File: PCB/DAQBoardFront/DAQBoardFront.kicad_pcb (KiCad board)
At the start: 2 copper layers, 59.9 x 60.2 mm, 42 parts, among them IC2 LMR51430YDDCR, J2 53375-0410, U5 TCAN1051VDRQ1

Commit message: Updated A-A filters w/ final version, updated BOM
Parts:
- C8: value C3216X5R1E476M160AC -> C3216X5R1E476MTJ00E
- L1, L2: value 10u -> 22u
- L3: value L -> 22u
- R1, R2: value 1.69k -> 6.57k
- R3: value R -> 26.4k
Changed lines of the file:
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@@
 			(layer "F.SilkS")
 		)
+		(fp_rect
+			(start -3 -2.5)
+			(end 18 51)
+			(stroke
+				(width 0.1)
+				(type solid)
+			)
+			(fill no)
+			(layer "F.CrtYd")
+		)
 		(fp_text user "${REFERENCE}"
 			(at 7.64 6.7 0)
@@
 			)
 		)
-		(property "Description" "Resistor, 60Ohm, 1%, 1/4W"
+		(property "Description" "RCS060359R0FKEA"
 			(at 0 0 90)
 			(layer "B.Fab")
@@
 			)
 		)
-		(attr smd)
+		(attr smd dnp)
 		(duplicate_pad_numbers_are_jumpers no)
 		(fp_line
@@
 			)
 		)
-		(property "Value" "C3216X5R1E476M160AC"
+		(property "Value" "C3216X5R1E476MTJ00E"
 			(at 0 -1.85 90)
 			(layer "B.Fab")
@@
 			)
 		)
-		(property "Value" "10u"
+		(property "Value" "22u"
 			(at 0 -1.55 90)
 			(layer "B.Fab")
@@
 			)
 		)
-		(property "Value" "1.69k"
+		(property "Value" "6.57k"
 			(at 0 -1.43 90)
 			(layer "B.Fab")
@@
 			)
 		)
-		(property "Description" "Resistor, 60Ohm, 1%, 1/4W"
+		(property "Description" "RCS060359R0FKEA"
 			(at 0 0 90)
 			(layer "B.Fab")
@@
 			)
 		)
-		(attr smd)
+		(attr smd dnp)
 		(duplicate_pad_numbers_are_jumpers no)
 		(fp_line
@@
 			)
 		)
-		(property "Value" "R"
+		(property "Value" "26.4k"
 			(at 0 -1.43 90)
 			(layer "B.Fab")
@@
 		)
 		(pad "2" smd rect
-			(at 1.15 0 180)
+			(at 1.15 0)
 			(size 0.42 0.82)
 			(layers "B.Cu" "B.Mask" "B.Paste")
@@
 			)
 		)
-		(property "Value" "10u"
+		(property "Value" "22u"
 			(at 0 -1.5 90)
 			(layer "B.Fab")
@@
 			)
 		)
-		(property "Value" "1.69k"
+		(property "Value" "6.57k"
 			(at 0 -1.43 90)
 			(layer "B.Fab")
@@
 			)
 		)
-		(property "Value" "L"
+		(property "Value" "22u"
 			(at 0 -1.55 90)
 			(layer "B.Fab")

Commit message: Finalized A-A filters, finishing touches on DAQ and Dash boards
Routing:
- net /GND: vias 18 -> 26
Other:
- board text added: "A-A Filters"
- board text added: "CAN Transceiver"
- board text added: "Current Sense"
- board text added: "Volt Step-Dn"
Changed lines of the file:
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@@
 		(tags "capacitor")
 		(property "Reference" "C1"
-			(at -0.05 -1.5 0)
+			(at -2.3 0.6 0)
 			(layer "B.SilkS")
 			(effects
@@
 	)
 	(gr_rect
+		(start 99.45 69.1)
+		(end 119.9 81.3)
+		(stroke
+			(width 0.1)
+			(type default)
+		)
+		(fill no)
+		(layer "B.SilkS")
+	)
+	(gr_rect
+		(start 105.45 81.4)
+		(end 125.9 101.9)
+		(stroke
+			(width 0.1)
+			(type default)
+		)
+		(fill no)
+		(layer "B.SilkS")
+	)
+	(gr_rect
+		(start 135.65 100.8)
+		(end 157.2 124.3)
+		(stroke
+			(width 0.1)
+			(type default)
+		)
+		(fill no)
+		(layer "B.SilkS")
+	)
+	(gr_rect
+		(start 136.35 75.35)
+		(end 157.5 97.8)
+		(stroke
+			(width 0.1)
+			(type default)
+		)
+		(fill no)
+		(layer "B.SilkS")
+	)
+	(gr_rect
 		(start 98.5 67.9)
 		(end 158.45 128.05)
@@
 		(layer "F.CrtYd")
 	)
+	(gr_text "CAN Transceiver"
+		(at 119.85 70.6 0)
+		(layer "B.SilkS")
+		(effects
+			(font
+				(size 1 1)
+				(thickness 0.1)
+			)
+			(justify left bottom mirror)
+		)
+	)
+	(gr_text "Current Sense"
+		(at 119.05 103.7 0)
+		(layer "B.SilkS")
+		(effects
+			(font
+				(size 1 1)
+				(thickness 0.125)
+			)
+			(justify left bottom mirror)
+		)
+	)
+	(gr_text "A-A Filters"
+		(at 144.2 125.85 0)
+		(layer "B.SilkS")
+		(effects
+			(font
+				(size 1 1)
+				(thickness 0.125)
+			)
+			(justify left bottom mirror)
+		)
+	)
+	(gr_text "Volt Step-Dn"
+		(at 147.2 77.15 0)
+		(layer "B.SilkS")
+		(effects
+			(font
+				(size 1 1)
+				(thickness 0.125)
+			)
+			(justify left bottom mirror)
+		)
+	)
 	(gr_text "BUCK 12V->5V"
-		(at 124.2 103.2 0)
+		(at 127.6 82.05 90)
 		(layer "B.SilkS")
 		(effects
@@
 	)
 	(via
+		(at 100.8 126.1)
+		(size 0.6)
+		(drill 0.3)
+		(layers "F.Cu" "B.Cu")
+		(free yes)
+		(net "/GND")
+	)
+	(via
 		(at 145.89 117.6725)
 		(size 0.6)
@@
 	)
 	(via
+		(at 157.15 75.95)
+		(size 0.6)
+		(drill 0.3)
+		(layers "F.Cu" "B.Cu")
+		(free yes)
+		(net "/GND")
+	)
+	(via
 		(at 143.89 110.5225)
 		(size 0.6)
@@
 	)
 	(via
+		(at 110.6 94.1)
+		(size 0.6)
+		(drill 0.3)
+		(layers "F.Cu" "B.Cu")
+		(free yes)
+		(net "/GND")
+	)
+	(via
 		(at 109.6 83.6)
 		(size 0.6)
@@
 	)
 	(via
+		(at 157.2 119.5)
+		(size 0.6)
+		(drill 0.3)
+		(layers "F.Cu" "B.Cu")
+		(free yes)
+		(net "/GND")
+	)
+	(via
 		(at 130.65 82.5)
 		(size 0.6)
@@
 	)
 	(via
+		(at 149.75 126.85)
+		(size 0.6)
+		(drill 0.3)
+		(layers "F.Cu" "B.Cu")
+		(free yes)
+		(net "/GND")
+	)
+	(via
 		(at 110.55 90.75)
 		(size 0.6)
@@
 	)
 	(via
+		(at 110.55 91.55)
+		(size 0.6)
+		(drill 0.3)
+		(layers "F.Cu" "B.Cu")
+		(free yes)
+		(net "/GND")
+	)
+	(via
 		(at 130.65 76.65)
 		(size 0.6)
 		(drill 0.3)
+		(layers "F.Cu" "B.Cu")
+		(free yes)
+		(net "/GND")
+	)
+	(via
+		(at 149.3 69.2)
+		(size 0.6)
+		(drill 0.3)
+		(layers "F.Cu" "B.Cu")
+		(free yes)
+		(net "/GND")
+	)
+	(via
+		(at 107.15 69.35)
+		(size 0.6)
+		(drill 0.3)

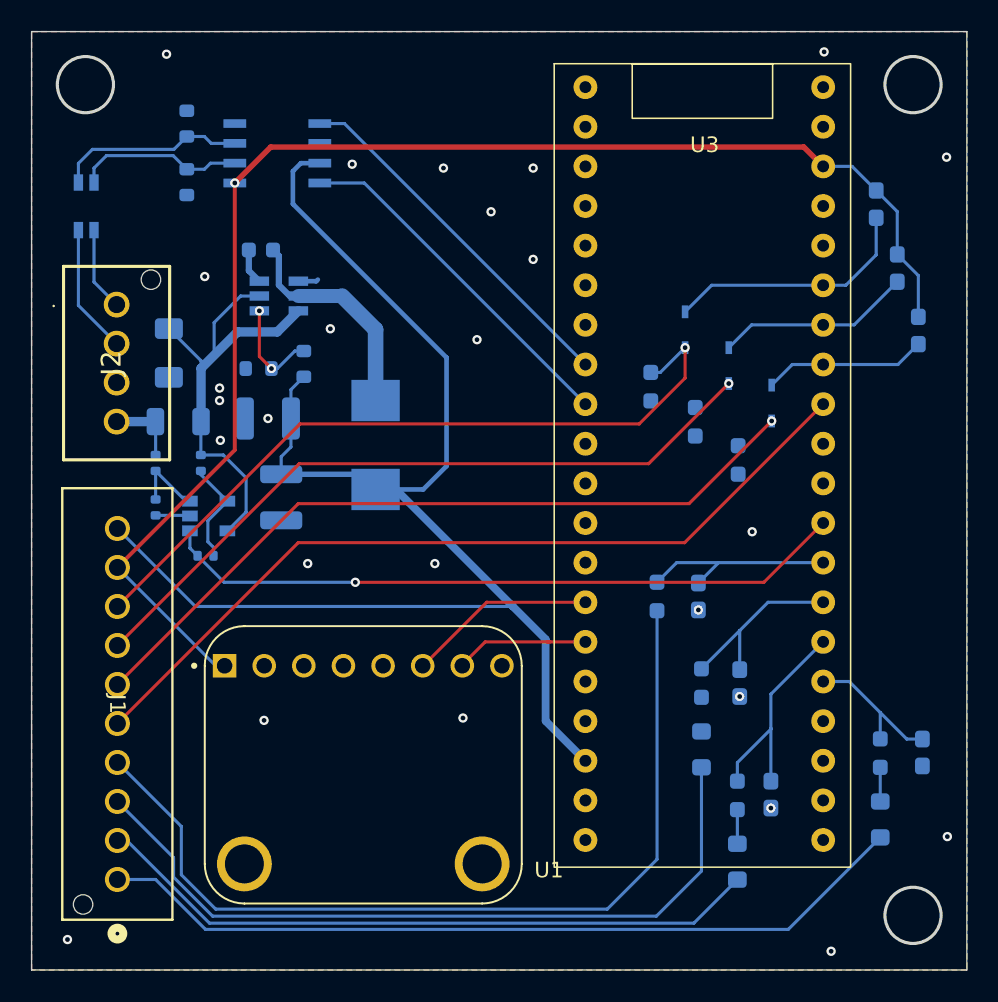
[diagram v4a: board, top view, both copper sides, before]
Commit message: Created hall effect test script for T4.1, adjusted hall effect input strategy
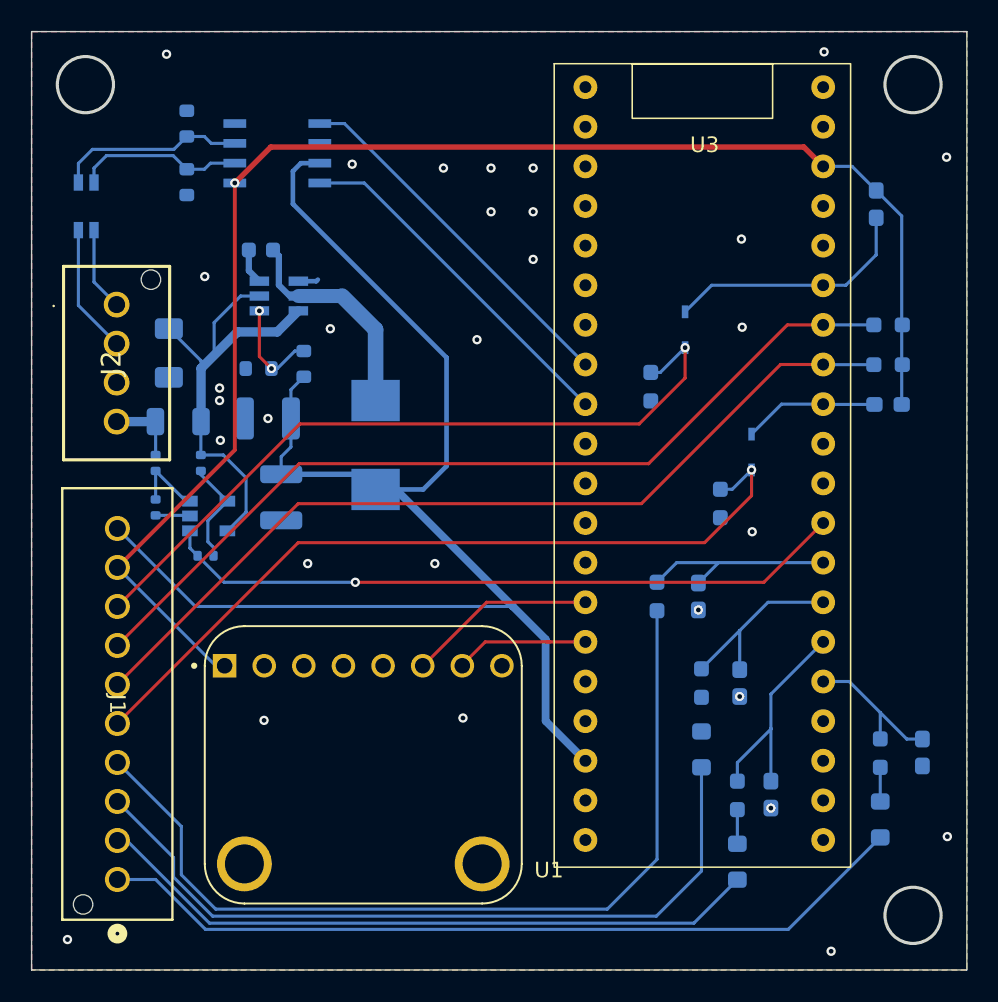
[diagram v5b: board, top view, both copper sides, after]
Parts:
- removed D4: 1N4148WS, CFR-Footprint-Library:SODFL2512X90N
- C4: value C -> 1u
- R10, R8: value 2k -> 1k
- R9: value 24k -> 2k; footprint LED_SMD:LED_0603_1608Metric_Pad1.05x0.95mm_HandSolder -> Resistor_SMD:R_0603_1608Metric_Pad0.98x0.95mm_HandSolder
- moved R9 16.9 mm to (142.7, 98.2)
- moved R8 13.8 mm to (153.4, 86.7), turned to 0 degrees
- moved R10 11.4 mm to (153.4, 89.2), turned to 0 degrees
- moved R7 8.76 mm to (153.4, 91.8), turned to 0 degrees
- moved D3 5.73 mm to (144.7, 94.8)
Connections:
- D3 pad 1: /FLHallEffect -> /ExtraDigital
- R10 pad 1: /GND -> /FRHallEffect
- R10 pad 2: /FRHallEffect -> /+3.3V
- R8 pad 1: /GND -> /FLHallEffect
- R8 pad 2: /FLHallEffect -> /+3.3V
- R9 pad 1: Net-(D4-A) -> /GND
- R9 pad 2: /+3.3V -> /ExtraDigital
- U3 pad 32: /ExtraDigital -> Net-(D3-A)
- U3 pad 33: Net-(D4-A) -> /FRHallEffect
- U3 pad 34: Net-(D3-A) -> /FLHallEffect
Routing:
- net /FLHallEffect: track 46.1 -> 57.0 mm, vias 1 -> 0
- net Net-(D4-A): track 10.5 -> 0.00 mm
- net /FRHallEffect: track 48.9 -> 57.0 mm, vias 1 -> 0
- net /+3.3V: track 89.7 -> 94.9 mm
- net Net-(D3-A): track 12.6 -> 8.68 mm
- net /ExtraDigital: track 53.7 -> 50.9 mm, vias 0 -> 1
- net /GND: vias 26 -> 30

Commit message: Added status LEDs to the DAQ board
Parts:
- added H1: MountingHole_Pad, Connector_PinHeader_1.00mm:PinHeader_1x01_P1.00mm_Vertical, F.Cu at (153.5, 107.2)
- added H2: MountingHole_Pad, Connector_PinHeader_1.00mm:PinHeader_1x01_P1.00mm_Vertical, F.Cu at (155.8, 107.2)
- added H3: MountingHole_Pad, Connector_PinHeader_1.00mm:PinHeader_1x01_P1.00mm_Vertical, F.Cu at (155.8, 103.2)
- added H4: MountingHole_Pad, Connector_PinHeader_1.00mm:PinHeader_1x01_P1.00mm_Vertical, F.Cu at (153.5, 103.2)
- added R20: 1k, Resistor_SMD:R_0603_1608Metric_Pad0.98x0.95mm_HandSolder, B.Cu at (155.8, 96.7)
- added R21: 1k, Resistor_SMD:R_0603_1608Metric_Pad0.98x0.95mm_HandSolder, B.Cu at (153.7, 99.8)
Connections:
- U3 pad 30: unconnected-(U3-A5-Pad30) -> Net-(U3-A5)
- U3 pad 31: unconnected-(U3-A6-Pad31) -> Net-(U3-A6)
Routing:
- net Net-(U3-A6): track 0.00 -> 7.12 mm
- net Net-(H3-Pad1): track 0.00 -> 5.68 mm
- net Net-(U3-A5): track 0.00 -> 5.23 mm
- net Net-(H4-Pad1): track 0.00 -> 2.65 mm
- net /GND: vias 30 -> 32
